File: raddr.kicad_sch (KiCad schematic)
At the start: 6 parts, among them J1 Conn_01x04_MountingPin, J2 Conn_01x04_MountingPin, U1 PMS150C-U06

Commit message: Footprints
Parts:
- removed J1, J2: Conn_01x04_MountingPin, symbol Connector_Generic_MountingPin:Conn_01x04_MountingPin
- added J1, J3: Conn_01x04, Connector_PinSocket_2.54mm:PinSocket_1x04_P2.54mm_Vertical, symbol Connector_Generic:Conn_01x04
- C1: footprint (none) -> Capacitor_SMD:C_0402_1005Metric
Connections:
- net +5VD: now also J1.2 (Pin_2), J3.3 (Pin_3)
- net GND: now also J1.1 (Pin_1), J3.4 (Pin_4)
- net at LED1.2 (DOUT): now also J3.1 (Pin_1)
- net at LED1.3 (DIN): now also J1.4 (Pin_4)
- net at U1.1 (PA4): now also J1.3 (Pin_3)
- net at U1.6 (PA3): now also J3.2 (Pin_2)
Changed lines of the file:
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@@
 	(wire
 		(pts
-			(xy 170.18 68.58) (xy 171.45 68.58)
+			(xy 170.18 68.58) (xy 173.99 68.58)
 		)
 		(stroke
@@
 	(wire
 		(pts
-			(xy 147.32 71.12) (xy 171.45 71.12)
+			(xy 147.32 71.12) (xy 173.99 71.12)
 		)
 		(stroke
@@
 	(wire
 		(pts
-			(xy 163.83 76.2) (xy 171.45 76.2)
+			(xy 163.83 76.2) (xy 173.99 76.2)
 		)
 		(stroke
@@
 	(wire
 		(pts
-			(xy 171.45 73.66) (xy 156.21 73.66)
+			(xy 173.99 73.66) (xy 156.21 73.66)
 		)
 		(stroke
@@
 	)
 	(symbol
-		(lib_id "Connector_Generic_MountingPin:Conn_01x04_MountingPin")
+		(lib_name "Conn_01x04_1")
+		(lib_id "Connector_Generic:Conn_01x04")
 		(at 116.84 76.2 180)
 		(unit 1)
@@
 		(fields_autoplaced yes)
 		(property "Reference" "J1"
-			(at 114.3 73.3043 0)
-			(effects
-				(font
-					(size 1.27 1.27)
-				)
-				(justify left)
-			)
-		)
-		(property "Value" "Conn_01x04_MountingPin"
-			(at 114.3 75.8443 0)
-			(effects
-				(font
-					(size 1.27 1.27)
-				)
-				(justify left)
-			)
-		)
-		(property "Footprint" ""
+			(at 116.84 64.77 0)
+			(effects
+				(font
+					(size 1.27 1.27)
+				)
+			)
+		)
+		(property "Value" "Conn_01x04"
+			(at 116.84 67.31 0)
+			(effects
+				(font
+					(size 1.27 1.27)
+				)
+			)
+		)
+		(property "Footprint" "Connector_PinSocket_2.54mm:PinSocket_1x04_P2.54mm_Vertical"
 			(at 116.84 76.2 0)
 			(effects
@@
 			)
 		)
-		(property "Description" "Generic connectable mounting pin connector, single row, 01x04, script generated (kicad-library-utils/schlib/autogen/connector/)"
+		(property "Description" "Generic connector, single row, 01x04, script generated (kicad-library-utils/schlib/autogen/connector/)"
 			(at 116.84 76.2 0)
 			(effects
@@
 			)
 		)
-		(pin "MP"
+		(pin "4"
 		)
 		(pin "2"
 		)
-		(pin "4"
-		)
 		(pin "3"
 		)
@@
 		)
 		(instances
-			(project ""
+			(project "raddr"
 				(path "/9585471a-96c4-4019-bcf7-b3f1c776d0db"
 					(reference "J1")
@@
 	)
 	(symbol
-		(lib_id "Connector_Generic_MountingPin:Conn_01x04_MountingPin")
-		(at 176.53 71.12 0)
+		(lib_id "Connector_Generic:Conn_01x04")
+		(at 179.07 71.12 0)
 		(unit 1)
 		(exclude_from_sim no)
@@
 		(dnp no)
 		(fields_autoplaced yes)
-		(property "Reference" "J2"
-			(at 179.07 71.4755 0)
+		(property "Reference" "J3"
+			(at 181.61 71.1199 0)
 			(effects
 				(font
@@
 			)
 		)
-		(property "Value" "Conn_01x04_MountingPin"
-			(at 179.07 74.0155 0)
+		(property "Value" "Conn_01x04"
+			(at 181.61 73.6599 0)
 			(effects
 				(font
@@
 			)
 		)
-		(property "Footprint" ""
-			(at 176.53 71.12 0)
+		(property "Footprint" "Connector_PinSocket_2.54mm:PinSocket_1x04_P2.54mm_Vertical"
+			(at 179.07 71.12 0)
 			(effects
 				(font
@@
 		)
 		(property "Datasheet" "~"
-			(at 176.53 71.12 0)
-			(effects
-				(font
-					(size 1.27 1.27)
-				)
-				(hide yes)
-			)
-		)
-		(property "Description" "Generic connectable mounting pin connector, single row, 01x04, script generated (kicad-library-utils/schlib/autogen/connector/)"
-			(at 176.53 71.12 0)
-			(effects
-				(font
-					(size 1.27 1.27)
-				)
-				(hide yes)
-			)
-		)
-		(pin "MP"
+			(at 179.07 71.12 0)
+			(effects
+				(font
+					(size 1.27 1.27)
+				)
+				(hide yes)
+			)
+		)
+		(property "Description" "Generic connector, single row, 01x04, script generated (kicad-library-utils/schlib/autogen/connector/)"
+			(at 179.07 71.12 0)
+			(effects
+				(font
+					(size 1.27 1.27)
+				)
+				(hide yes)
+			)
+		)
+		(pin "4"
 		)
 		(pin "2"
 		)
-		(pin "4"
-		)
 		(pin "3"
 		)
@@
 		)
 		(instances
-			(project "raddr"
+			(project ""
 				(path "/9585471a-96c4-4019-bcf7-b3f1c776d0db"
-					(reference "J2")
+					(reference "J3")
 					(unit 1)
 				)
@@
 			)
 		)
-		(property "Footprint" ""
+		(property "Footprint" "Capacitor_SMD:C_0402_1005Metric"
 			(at 157.1752 86.36 0)
 			(effects

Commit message: add traces
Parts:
- removed J1, J3: Conn_01x04, Connector_PinSocket_2.54mm:PinSocket_1x04_P2.54mm_Vertical, symbol Connector_Generic:Conn_01x04
- added J1, J3: Conn_01x07, Connector_PinSocket_2.54mm:PinSocket_1x07_P2.54mm_Vertical, symbol Connector_Generic:Conn_01x07
- C1: footprint Capacitor_SMD:C_0402_1005Metric -> Capacitor_SMD:C_0603_1608Metric_Pad1.08x0.95mm_HandSolder
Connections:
- net +5VD: now also J1.4 (Pin_4), J3.4 (Pin_4)
- net GND: now also CH1.1, J1.5 (Pin_5), J3.5 (Pin_5); no longer CH1.2
- net at LED1.2 (DOUT): now also J1.7 (Pin_7)
- net at LED1.3 (DIN): now also J3.7 (Pin_7)
- net at U1.1 (PA4): now also J1.6 (Pin_6)
- net at U1.6 (PA3): now also CH1.2
- net at U1.3 (PA6): now also J3.6 (Pin_6)
- net at U1.4 (PA5): now also J3.3 (Pin_3); no longer CH1.1
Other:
- moved on the sheet: C1, CH1, U1

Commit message: Muck around about traces
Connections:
- net at LED1.2 (DOUT): now also J3.7 (Pin_7); no longer J1.7 (Pin_7)
- net at LED1.3 (DIN): now also J1.7 (Pin_7); no longer J3.7 (Pin_7)
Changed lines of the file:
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@@
+	(wire
+		(pts
+			(xy 157.48 68.58) (xy 121.92 68.58)
+		)
+		(stroke
+			(width 0)
+			(type default)
+		)
+	)
 	(wire
 		(pts
@@
 	(wire
 		(pts
-			(xy 173.99 68.58) (xy 173.99 57.15)
-		)
-		(stroke
-			(width 0)
-			(type default)
-		)
-	)
-	(wire
-		(pts
 			(xy 140.97 107.95) (xy 140.97 110.49)
 		)
@@
 	(wire
 		(pts
+			(xy 170.18 68.58) (xy 173.99 68.58)
+		)
+		(stroke
+			(width 0)
+			(type default)
+		)
+	)
+	(wire
+		(pts
 			(xy 121.92 76.2) (xy 161.29 76.2)
 		)
@@
 	(wire
 		(pts
+			(xy 157.48 63.5) (xy 157.48 68.58)
+		)
+		(stroke
+			(width 0)
+			(type default)
+		)
+	)
+	(wire
+		(pts
 			(xy 138.43 114.3) (xy 107.95 114.3)
 		)
@@
 	(wire
 		(pts
+			(xy 173.99 57.15) (xy 173.99 63.5)
+		)
+		(stroke
+			(width 0)
+			(type default)
+		)
+	)
+	(wire
+		(pts
 			(xy 154.94 96.52) (xy 154.94 86.36)
 		)
@@
 	(wire
 		(pts
+			(xy 121.92 57.15) (xy 121.92 66.04)
+		)
+		(stroke
+			(width 0)
+			(type default)
+		)
+	)
+	(wire
+		(pts
 			(xy 138.43 90.17) (xy 138.43 73.66)
 		)
@@
 	(wire
 		(pts
+			(xy 173.99 63.5) (xy 157.48 63.5)
+		)
+		(stroke
+			(width 0)
+			(type default)
+		)
+	)
+	(wire
+		(pts
 			(xy 107.95 49.53) (xy 146.05 49.53)
 		)
@@
 	(wire
 		(pts
-			(xy 121.92 68.58) (xy 121.92 57.15)
-		)
-		(stroke
-			(width 0)
-			(type default)
-		)
-	)
-	(wire
-		(pts
 			(xy 135.89 71.12) (xy 135.89 90.17)
 		)
@@
 	(wire
 		(pts
+			(xy 170.18 66.04) (xy 170.18 68.58)
+		)
+		(stroke
+			(width 0)
+			(type default)
+		)
+	)
+	(wire
+		(pts
 			(xy 161.29 49.53) (xy 161.29 76.2)
 		)
@@
 	(wire
 		(pts
+			(xy 121.92 66.04) (xy 170.18 66.04)
+		)
+		(stroke
+			(width 0)
+			(type default)
+		)
+	)
+	(wire
+		(pts
 			(xy 161.29 97.79) (xy 161.29 86.36)
 		)
@@
 		)
 	)
+	(label "gnd"
+		(at 111.76 74.93 0)
+		(fields_autoplaced yes)
+		(effects
+			(font
+				(size 1.27 1.27)
+			)
+			(justify left bottom)
+		)
+	)

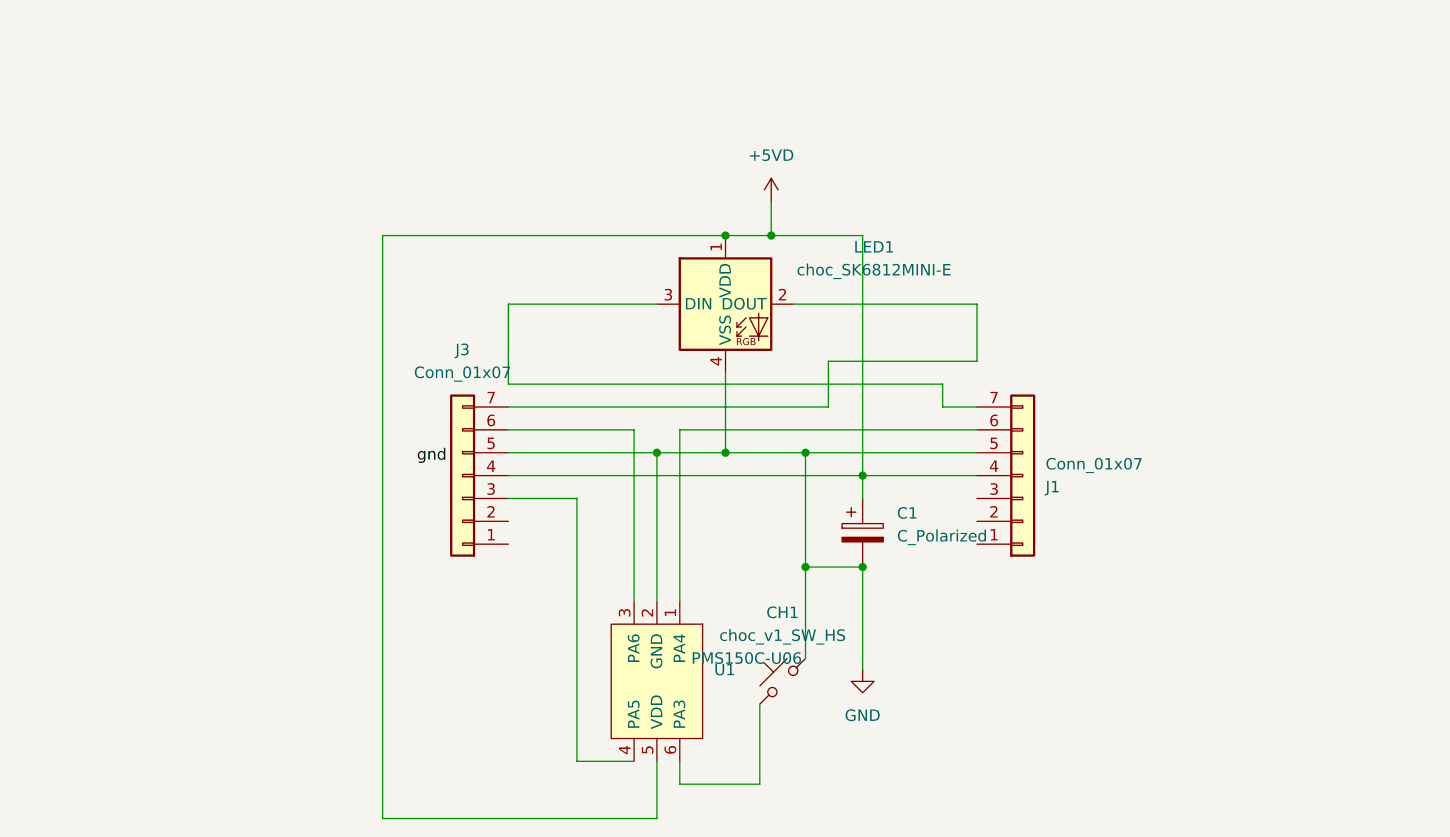
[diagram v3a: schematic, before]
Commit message: WFP correction factor
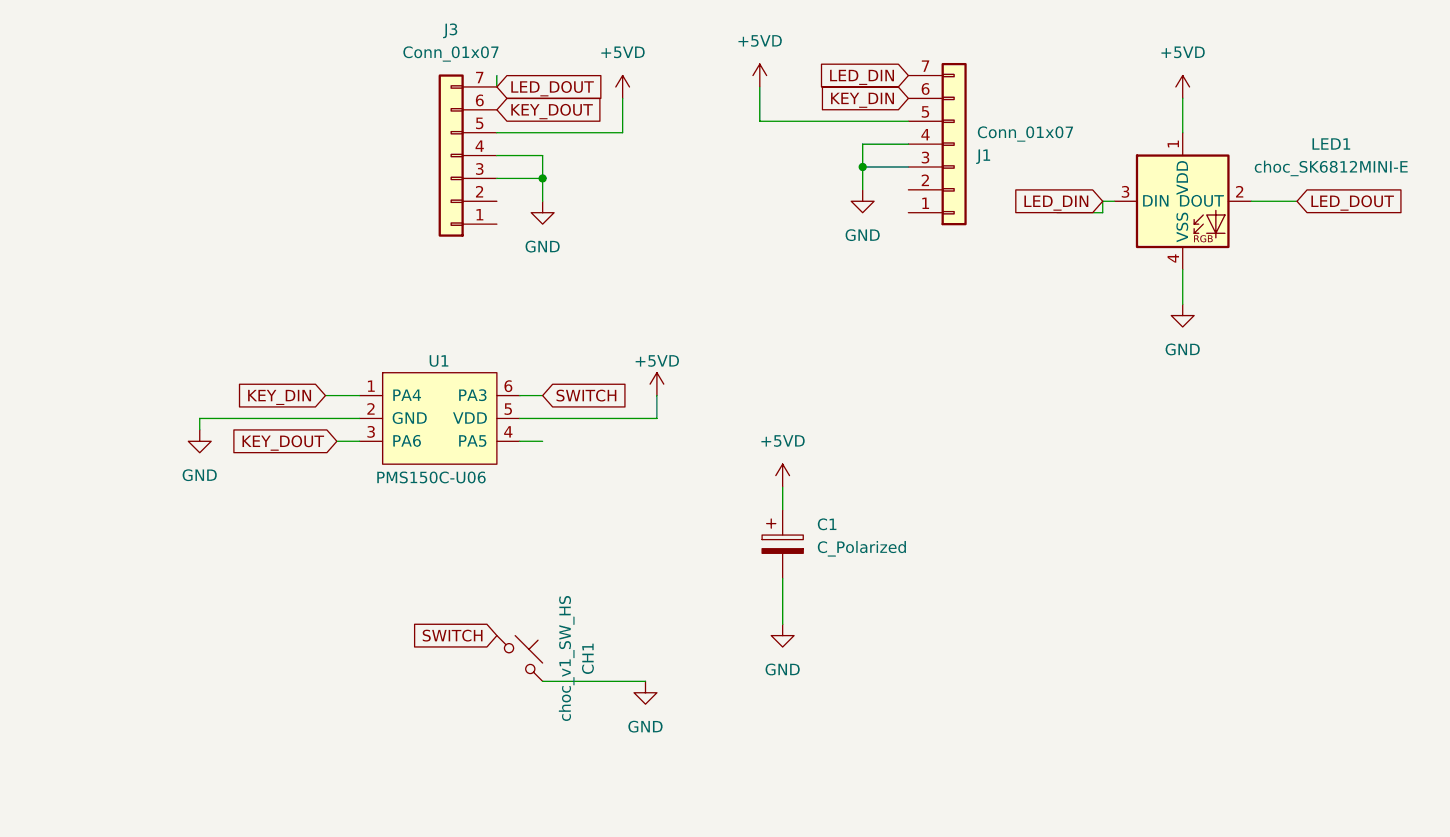
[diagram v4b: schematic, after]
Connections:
- net +5VD: now also J1.5 (Pin_5), J3.5 (Pin_5); no longer J1.4 (Pin_4), J3.4 (Pin_4)
- net GND: now also J1.3 (Pin_3), J1.4 (Pin_4), J3.3 (Pin_3), J3.4 (Pin_4); no longer J1.5 (Pin_5), J3.5 (Pin_5)
- net LED_DOUT: now reaches J3.7 (Pin_7), LED1.2 (DOUT)
- net LED_DIN: now reaches J1.7 (Pin_7), LED1.3 (DIN)
- net KEY_DIN: now reaches J1.6 (Pin_6), U1.1 (PA4)
- net at U1.4 (PA5): no longer J3.3 (Pin_3)
- net KEY_DOUT: now reaches J3.6 (Pin_6), U1.3 (PA6)
- net SWITCH: now reaches CH1.2, U1.6 (PA3)
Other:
- moved on the sheet: C1, CH1, J1, J3, LED1, U1

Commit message: split connector
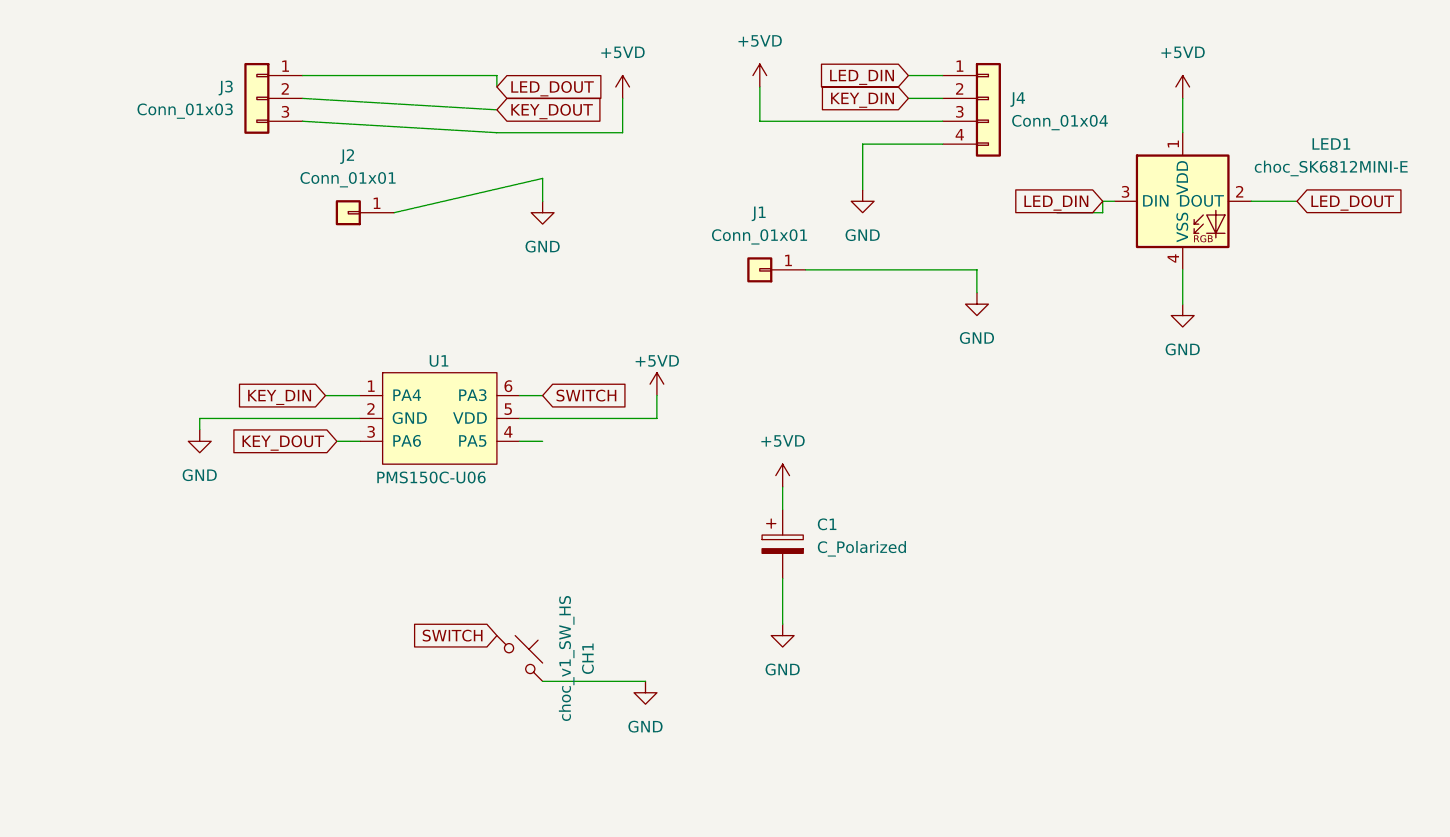
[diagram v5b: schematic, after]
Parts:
- removed J1, J3: Conn_01x07, Connector_PinSocket_2.54mm:PinSocket_1x07_P2.54mm_Vertical, symbol Connector_Generic:Conn_01x07
- added J1, J2: Conn_01x01, Connector_PinSocket_2.54mm:PinSocket_1x01_P2.54mm_Vertical, symbol Connector_Generic:Conn_01x01
- added J3: Conn_01x03, Connector_PinSocket_2.54mm:PinSocket_1x03_P2.54mm_Vertical, symbol Connector_Generic:Conn_01x03
- added J4: Conn_01x04, Connector_PinSocket_2.54mm:PinSocket_1x04_P2.54mm_Vertical, symbol Connector_Generic:Conn_01x04
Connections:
- net +5VD: now also J3.3 (Pin_3), J4.3 (Pin_3)
- net GND: now also J1.1 (Pin_1), J2.1 (Pin_1), J4.4 (Pin_4)
- net KEY_DIN: now also J4.2 (Pin_2)
- net KEY_DOUT: now also J3.2 (Pin_2)
- net LED_DIN: now also J4.1 (Pin_1)
- net LED_DOUT: now also J3.1 (Pin_1)

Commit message: silk screen
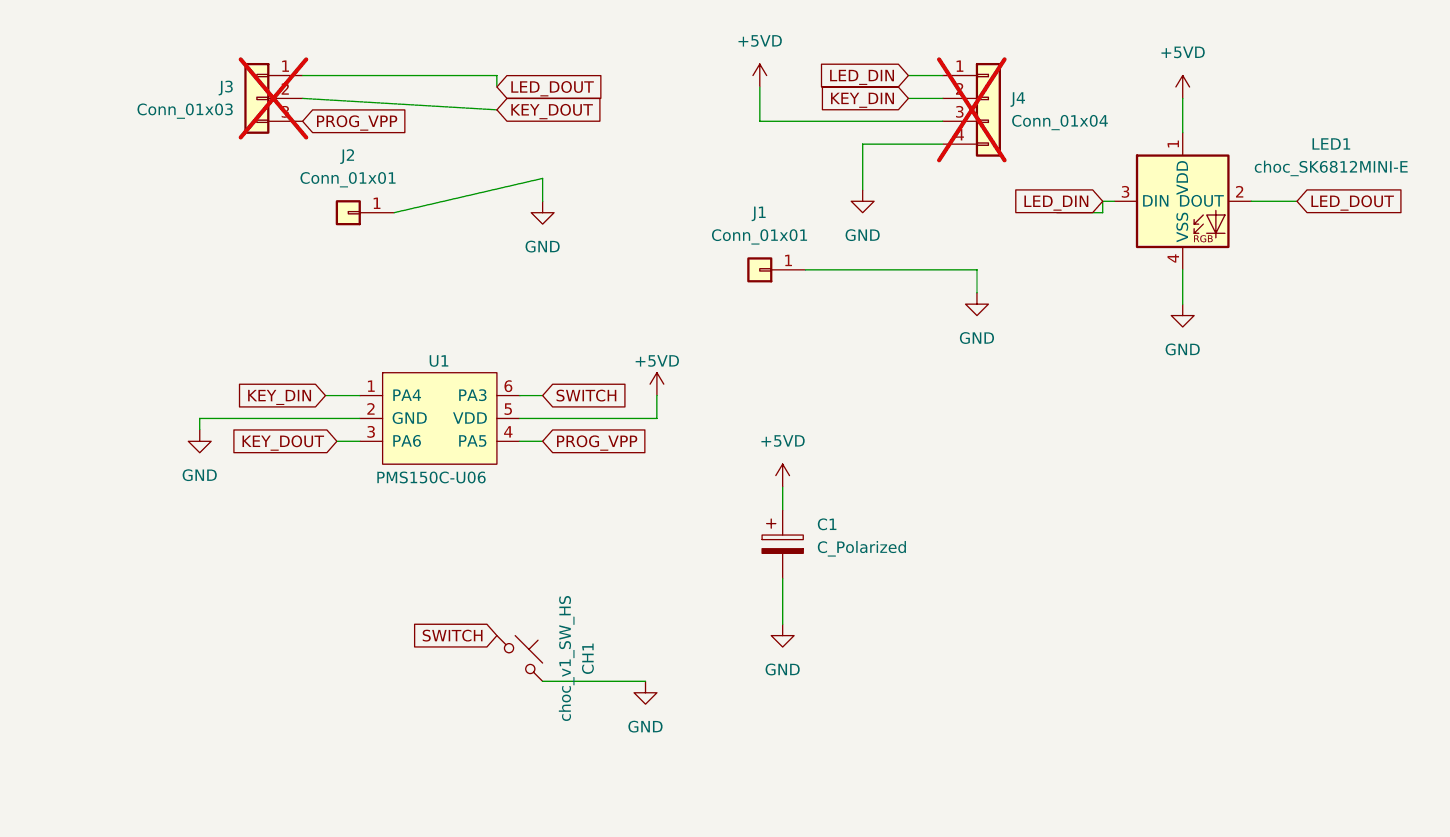
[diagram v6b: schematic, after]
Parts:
- J3, J4: now not fitted
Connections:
- net +5VD: no longer J3.3 (Pin_3)
- net PROG_VPP: now reaches U1.4 (PA5)
- net PROG_VPP: now also J3.3 (Pin_3)
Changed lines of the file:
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@@
-	(wire
-		(pts
-			(xy 134.62 34.29) (xy 134.62 38.1)
-		)
-		(stroke
-			(width 0)
-			(type default)
-		)
-	)
 	(wire
 		(pts
@@
 	(wire
 		(pts
-			(xy 120.65 38.1) (xy 134.62 38.1)
-		)
-		(stroke
-			(width 0)
-			(type default)
-		)
-	)
-	(wire
-		(pts
 			(xy 204.47 45.72) (xy 209.55 45.72)
 		)
@@
 		(pts
 			(xy 125.73 45.72) (xy 125.73 43.18)
-		)
-		(stroke
-			(width 0)
-			(type default)
-		)
-	)
-	(wire
-		(pts
-			(xy 99.06 36.83) (xy 120.65 38.1)
 		)
 		(stroke
@@
 		)
 	)
+	(global_label "PROG_VPP"
+		(shape input)
+		(at 99.06 36.83 0)
+		(fields_autoplaced yes)
+		(effects
+			(font
+				(size 1.27 1.27)
+			)
+			(justify left)
+		)
+		(property "Intersheetrefs" "${INTERSHEET_REFS}"
+			(at 106.2784 36.83 0)
+			(effects
+				(font
+					(size 1.27 1.27)
+				)
+				(justify left)
+				(hide yes)
+			)
+		)
+	)
 	(global_label "SWITCH"
 		(shape input)
@@
 		)
 	)
+	(global_label "PROG_VPP"
+		(shape input)
+		(at 125.73 72.39 0)
+		(fields_autoplaced yes)
+		(effects
+			(font
+				(size 1.27 1.27)
+			)
+			(justify left)
+		)
+		(property "Intersheetrefs" "${INTERSHEET_REFS}"
+			(at 132.9484 72.39 0)
+			(effects
+				(font
+					(size 1.27 1.27)
+				)
+				(justify left)
+				(hide yes)
+			)
+		)
+	)
 	(global_label "LED_DIN"
 		(shape input)
@@
 		(in_bom yes)
 		(on_board yes)
-		(dnp no)
+		(dnp yes)
 		(property "Reference" "J3"
 			(at 91.44 33.0199 0)
@@
 		(in_bom yes)
 		(on_board yes)
-		(dnp no)
+		(dnp yes)
 		(fields_autoplaced yes)
 		(property "Reference" "J4"
@@
 					(unit 1)
 				)
-			)
-		)
-	)
-	(symbol
-		(lib_id "power:+5VD")
-		(at 134.62 34.29 0)
-		(unit 1)
-		(exclude_from_sim no)
-		(in_bom yes)
-		(on_board yes)
-		(dnp no)
-		(property "Reference" "#PWR01"
-			(at 134.62 38.1 0)
-			(effects
-				(font
-					(size 1.27 1.27)
-				)
-				(hide yes)
-			)
-		)
-		(property "Value" "+5VD"
-			(at 134.62 29.21 0)
-			(effects
-				(font
-					(size 1.27 1.27)
-				)
-			)
-		)
-		(property "Footprint" ""
-			(at 134.62 34.29 0)
-			(effects
-				(font
-					(size 1.27 1.27)
-				)
-				(hide yes)
-			)
-		)
-		(property "Datasheet" ""
-			(at 134.62 34.29 0)
-			(effects
-				(font
-					(size 1.27 1.27)
-				)
-				(hide yes)
-			)
-		)
-		(property "Description" "Power symbol creates a global label with name \"+5VD\""
-			(at 134.62 34.29 0)
-			(effects
-				(font
-					(size 1.27 1.27)
-				)
-				(hide yes)
-			)
-		)
-		(pin "1"
-		)
-		(instances
-			(project ""
-				(path "/9585471a-96c4-4019-bcf7-b3f1c776d0db"
-					(reference "#PWR01")
-					(unit 1)
-				)

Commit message: Silk screen adjustments.
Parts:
- renumbered J3 to J1, J4 to J3, J1 to J4
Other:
- moved on the sheet: C1, CH1, J1, J2, J3, J4, LED1, U1
